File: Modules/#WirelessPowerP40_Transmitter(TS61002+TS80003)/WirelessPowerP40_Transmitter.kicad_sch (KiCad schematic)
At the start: 135 parts, among them J1 USBA, J2 I2C, J3 I2C, J4 Coil Therm, J5 COIL 20uH, J6 Conn_01x02_Male, J7 Conn_01x02_Male, U1 TS30041, U10 HUSB238, U2 TS94033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

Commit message: rollback (PD3.0 fix)
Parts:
- J1: footprint USB_plug:SHENZHEN-CHUANGQIN-TECHNOLOGY_CQ-USB-C16PSMT01 -> USB_plug:USB4125-GF-A_REVA2; symbol CQ-USB-C16PSMT01:CQ-USB-C16PSMT01 -> USB4125-GF-A_REVA2:USB4125-GF-A_REVA2; MANUFACTURER Shenzhen Chuangpin Science and Technology -> GCT; MAXIMUM_PACKAGE_HEIGHT 3.36mm -> 3.16 mm; PARTREV A -> Rev A2
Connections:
- net +24V: now also J1.A9 (VBUS), J1.B9 (VBUS); no longer J1.A4_B9 (VBUS), J1.B4_A9 (VBUS)
- net GND: now also J1.A12 (GND), J1.B12 (GND); no longer J1.A1_B12 (GND), J1.B1_A12 (GND)
- removed net D+: J1.A6 (DP1), J1.B6 (DP2), U10.2 (D+)
- removed net D-: J1.A7 (DN1), J1.B7 (DN2), U10.3 (D-)
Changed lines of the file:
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@@
   (junction (at 375.92 85.09) (diameter 0) (color 0 0 0 0))
   (junction (at 388.62 213.36) (diameter 0) (color 0 0 0 0))
-  (no_connect (at 26.67 54.61))
-  (no_connect (at 26.67 57.15))
   (no_connect (at 49.53 104.14))
   (no_connect (at 62.23 257.81))
+  (no_connect (at 147.32 40.64))
+  (no_connect (at 147.32 44.45))
   (no_connect (at 165.1 36.83))
   (no_connect (at 165.1 40.64))
@@
   (no_connect (at 243.84 255.27))
   (no_connect (at 243.84 257.81))
-  (wire (pts (xy 26.67 43.18) (xy 26.67 45.72))
-    (stroke (width 0) (type default) (color 0 0 0 0))
-  )
-  (wire (pts (xy 26.67 48.26) (xy 26.67 50.8))
-    (stroke (width 0) (type default) (color 0 0 0 0))
-  )
   (wire (pts (xy 30.48 214.63) (xy 34.29 214.63))
     (stroke (width 0.5) (type default) (color 255 1 18 1))
@@
     (effects (font (size 1.27 1.27)) (justify left bottom))
   )
-  (global_label "CC1" (shape input) (at 26.67 38.1 180) (fields_autoplaced)
-    (effects (font (size 1.27 1.27)) (justify right))
-    (property "Intersheet References" "${INTERSHEET_REFS}" (id 0) (at 20.5074 38.0206 0)
-      (effects (font (size 1.27 1.27)) (justify right) hide)
-    )
-  )
-  (global_label "CC2" (shape input) (at 26.67 40.64 180) (fields_autoplaced)
-    (effects (font (size 1.27 1.27)) (justify right))
-    (property "Intersheet References" "${INTERSHEET_REFS}" (id 0) (at 20.5074 40.5606 0)
-      (effects (font (size 1.27 1.27)) (justify right) hide)
-    )
-  )
-  (global_label "D+" (shape input) (at 26.67 44.45 180) (fields_autoplaced)
-    (effects (font (size 1.27 1.27)) (justify right))
-    (property "Intersheet References" "${INTERSHEET_REFS}" (id 0) (at 21.4145 44.3706 0)
-      (effects (font (size 1.27 1.27)) (justify right) hide)
-    )
-  )
-  (global_label "D-" (shape input) (at 26.67 49.53 180) (fields_autoplaced)
-    (effects (font (size 1.27 1.27)) (justify right))
-    (property "Intersheet References" "${INTERSHEET_REFS}" (id 0) (at 21.4145 49.4506 0)
-      (effects (font (size 1.27 1.27)) (justify right) hide)
-    )
-  )
   (global_label "COIL-" (shape input) (at 30.48 214.63 180) (fields_autoplaced)
     (effects (font (size 1.27 1.27)) (justify right))
@@
     )
   )
+  (global_label "CC1" (shape input) (at 50.8 44.45 0) (fields_autoplaced)
+    (effects (font (size 1.27 1.27)) (justify left))
+    (property "Intersheet References" "${INTERSHEET_REFS}" (id 0) (at 56.9626 44.3706 0)
+      (effects (font (size 1.27 1.27)) (justify left) hide)
+    )
+  )
+  (global_label "CC2" (shape input) (at 50.8 46.99 0) (fields_autoplaced)
+    (effects (font (size 1.27 1.27)) (justify left))
+    (property "Intersheet References" "${INTERSHEET_REFS}" (id 0) (at 56.9626 46.9106 0)
+      (effects (font (size 1.27 1.27)) (justify left) hide)
+    )
+  )
   (global_label "DRV_EN" (shape input) (at 52.07 156.21 180) (fields_autoplaced)
     (effects (font (size 1.27 1.27)) (justify right))
@@
     )
   )
-  (global_label "D+" (shape input) (at 147.32 40.64 180) (fields_autoplaced)
-    (effects (font (size 1.27 1.27)) (justify right))
-    (property "Intersheet References" "${INTERSHEET_REFS}" (id 0) (at 142.0645 40.5606 0)
-      (effects (font (size 1.27 1.27)) (justify right) hide)
-    )
-  )
-  (global_label "D-" (shape input) (at 147.32 44.45 180) (fields_autoplaced)
-    (effects (font (size 1.27 1.27)) (justify right))
-    (property "Intersheet References" "${INTERSHEET_REFS}" (id 0) (at 142.0645 44.3706 0)
-      (effects (font (size 1.27 1.27)) (justify right) hide)
-    )
-  )
   (global_label "CC1" (shape input) (at 147.32 48.26 180) (fields_autoplaced)
     (effects (font (size 1.27 1.27)) (justify right))
@@
     (pin "7")
   )
+  (symbol (lib_id "USB4125-GF-A_REVA2:USB4125-GF-A_REVA2") (at 38.1 46.99 0) (mirror y) (unit 1)
+    (in_bom yes) (on_board yes)
+    (property "Reference" "J1" (id 0) (at 38.1 30.48 0))
+    (property "Value" "USBA" (id 1) (at 38.1 33.02 0))
+    (property "Footprint" "USB_plug:USB4125-GF-A_REVA2" (id 2) (at 38.1 46.99 0)
+      (effects (font (size 1.27 1.27)) (justify left bottom) hide)
+    )
+    (property "Datasheet" " ~" (id 3) (at 38.1 46.99 0)
+      (effects (font (size 1.27 1.27)) (justify left bottom) hide)
+    )
+    (property "MAXIMUM_PACKAGE_HEIGHT" "3.16 mm" (id 4) (at 38.1 46.99 0)
+      (effects (font (size 1.27 1.27)) (justify left bottom) hide)
+    )
+    (property "STANDARD" "Manufacturer Recommendations" (id 5) (at 38.1 46.99 0)
+      (effects (font (size 1.27 1.27)) (justify left bottom) hide)
+    )
+    (property "PARTREV" "Rev A2" (id 6) (at 38.1 46.99 0)
+      (effects (font (size 1.27 1.27)) (justify left bottom) hide)
+    )
+    (property "MANUFACTURER" "GCT" (id 7) (at 38.1 46.99 0)
+      (effects (font (size 1.27 1.27)) (justify left bottom) hide)
+    )
+    (pin "A12")
+    (pin "A5")
+    (pin "A9")
+    (pin "B12")
+    (pin "B5")
+    (pin "B9")
+    (pin "S1")
+    (pin "S2")
+    (pin "S3")
+    (pin "S4")
+  )
   (symbol (lib_id "TS:TS94033") (at 67.31 152.4 0) (unit 1)
     (in_bom yes) (on_board yes) (fields_autoplaced)
@@
     (pin "9")
   )
-  (symbol (lib_id "CQ-USB-C16PSMT01:CQ-USB-C16PSMT01") (at 38.1 45.72 0) (unit 1)
-    (in_bom yes) (on_board yes)
-    (property "Reference" "J1" (id 0) (at 38.1 29.21 0))
-    (property "Value" "USBA" (id 1) (at 38.1 31.75 0))
-    (property "Footprint" "USB_plug:SHENZHEN-CHUANGQIN-TECHNOLOGY_CQ-USB-C16PSMT01" (id 2) (at 38.1 45.72 0)
-      (effects (font (size 1.27 1.27)) (justify left bottom) hide)
-    )
-    (property "Datasheet" " ~" (id 3) (at 38.1 45.72 0)
-      (effects (font (size 1.27 1.27)) (justify left bottom) hide)
-    )
-    (property "MAXIMUM_PACKAGE_HEIGHT" "3.36mm" (id 4) (at 38.1 45.72 0)
-      (effects (font (size 1.27 1.27)) (justify left bottom) hide)
-    )
-    (property "STANDARD" "Manufacturer Recommendations" (id 5) (at 38.1 45.72 0)
-      (effects (font (size 1.27 1.27)) (justify left bottom) hide)
-    )
-    (property "PARTREV" "A" (id 6) (at 38.1 45.72 0)
-      (effects (font (size 1.27 1.27)) (justify left bottom) hide)
-    )
-    (property "MANUFACTURER" "Shenzhen Chuangpin Science and Technology" (id 7) (at 38.1 45.72 0)
-      (effects (font (size 1.27 1.27)) (justify left bottom) hide)
-    )
-    (pin "A1_B12")
-    (pin "A4_B9")
-    (pin "A5")
-    (pin "A6")
-    (pin "A7")
-    (pin "A8")
-    (pin "B1_A12")
-    (pin "B4_A9")
-    (pin "B5")
-    (pin "B6")
-    (pin "B7")
-    (pin "B8")
-    (pin "S1")
-    (pin "S2")
-    (pin "S3")
-    (pin "S4")
-  )
   (symbol (lib_id "TS:TS61002") (at 248.92 85.09 0) (unit 1)
     (in_bom yes) (on_board yes) (fields_autoplaced)
@@
     )
     (path "/aadfb580-07ac-4146-909c-e21612e4a910"
-      (reference "J1") (unit 1) (value "USBA") (footprint "USB_plug:SHENZHEN-CHUANGQIN-TECHNOLOGY_CQ-USB-C16PSMT01")
+      (reference "J1") (unit 1) (value "USBA") (footprint "USB_plug:USB4125-GF-A_REVA2")
     )
     (path "/315aa701-aff7-4924-b211-8b9bbfa38ab3"

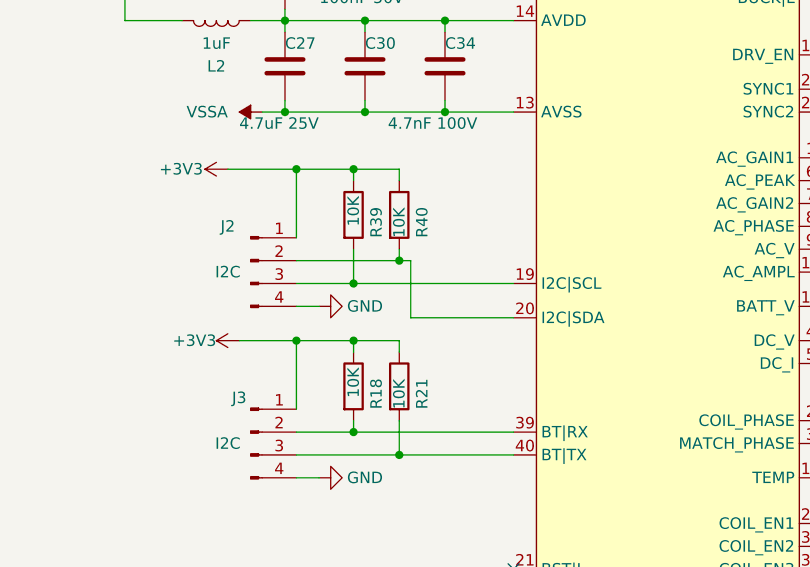
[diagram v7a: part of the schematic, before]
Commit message: IO silk label fix
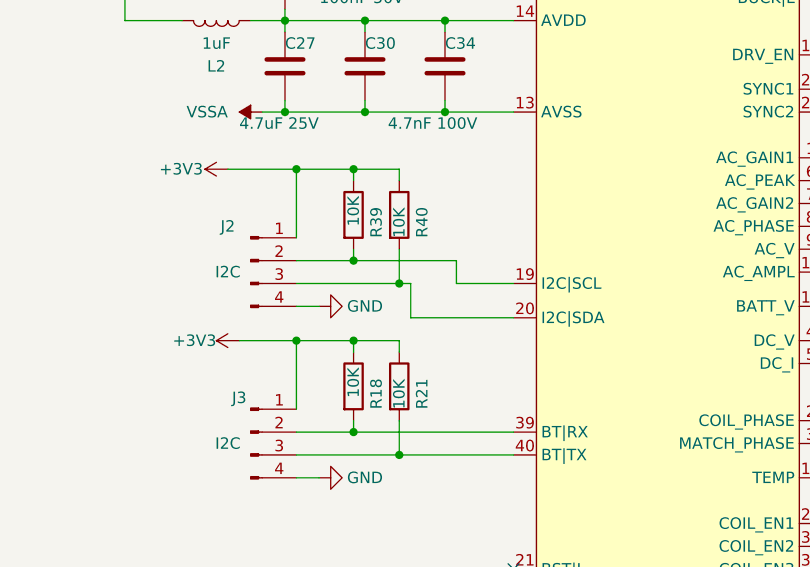
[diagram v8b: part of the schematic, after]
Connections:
- net at R40.2, U5.20 (I2C|SDA): now also J2.3 (Pin_3); no longer J2.2 (Pin_2)
- net at R39.2, U5.19 (I2C|SCL): now also J2.2 (Pin_2); no longer J2.3 (Pin_3)
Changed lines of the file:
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@@
   (junction (at 185.42 232.41) (diameter 0) (color 0 0 0 0))
   (junction (at 191.77 213.36) (diameter 0) (color 0 0 0 0))
-  (junction (at 191.77 226.06) (diameter 0) (color 0 0 0 0))
+  (junction (at 191.77 223.52) (diameter 0) (color 0 0 0 0))
   (junction (at 191.77 232.41) (diameter 0) (color 0 0 0 0))
   (junction (at 191.77 242.57) (diameter 0) (color 0 0 0 0))
@@
   (junction (at 193.04 196.85) (diameter 0) (color 0 0 0 0))
   (junction (at 193.04 207.01) (diameter 0) (color 0 0 0 0))
-  (junction (at 196.85 223.52) (diameter 0) (color 0 0 0 0))
+  (junction (at 196.85 226.06) (diameter 0) (color 0 0 0 0))
   (junction (at 196.85 245.11) (diameter 0) (color 0 0 0 0))
   (junction (at 200.66 123.19) (diameter 0) (color 0 0 0 0))
@@
     (stroke (width 0) (type default) (color 0 0 0 0))
   )
-  (wire (pts (xy 185.42 223.52) (xy 196.85 223.52))
+  (wire (pts (xy 185.42 223.52) (xy 191.77 223.52))
+    (stroke (width 0) (type default) (color 0 0 0 0))
+  )
+  (wire (pts (xy 185.42 226.06) (xy 196.85 226.06))
     (stroke (width 0) (type default) (color 0 0 0 0))
   )
@@
     (stroke (width 0) (type default) (color 0 0 0 0))
   )
-  (wire (pts (xy 191.77 222.25) (xy 191.77 226.06))
-    (stroke (width 0) (type default) (color 0 0 0 0))
-  )
-  (wire (pts (xy 191.77 226.06) (xy 185.42 226.06))
-    (stroke (width 0) (type default) (color 0 0 0 0))
-  )
-  (wire (pts (xy 191.77 226.06) (xy 209.55 226.06))
+  (wire (pts (xy 191.77 222.25) (xy 191.77 223.52))
+    (stroke (width 0) (type default) (color 0 0 0 0))
+  )
+  (wire (pts (xy 191.77 223.52) (xy 203.2 223.52))
     (stroke (width 0) (type default) (color 0 0 0 0))
   )
@@
     (stroke (width 0) (type default) (color 0 0 0 0))
   )
-  (wire (pts (xy 196.85 222.25) (xy 196.85 223.52))
-    (stroke (width 0) (type default) (color 0 0 0 0))
-  )
-  (wire (pts (xy 196.85 223.52) (xy 198.12 223.52))
+  (wire (pts (xy 196.85 222.25) (xy 196.85 226.06))
+    (stroke (width 0) (type default) (color 0 0 0 0))
+  )
+  (wire (pts (xy 196.85 226.06) (xy 198.12 226.06))
     (stroke (width 0) (type default) (color 0 0 0 0))
   )
@@
     (stroke (width 0) (type default) (color 0 0 0 0))
   )
-  (wire (pts (xy 198.12 223.52) (xy 198.12 229.87))
+  (wire (pts (xy 198.12 226.06) (xy 198.12 229.87))
     (stroke (width 0) (type default) (color 0 0 0 0))
   )
@@
     (stroke (width 0) (type default) (color 0 0 0 0))
   )
+  (wire (pts (xy 203.2 223.52) (xy 203.2 226.06))
+    (stroke (width 0) (type default) (color 0 0 0 0))
+  )
+  (wire (pts (xy 203.2 226.06) (xy 209.55 226.06))
+    (stroke (width 0) (type default) (color 0 0 0 0))
+  )
